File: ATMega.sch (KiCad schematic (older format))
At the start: 28 parts, among them J12 Conn_02x03_Odd_Even, SW1 SW_Push, U3 ATmega2560-16AU, Y1 16MHz

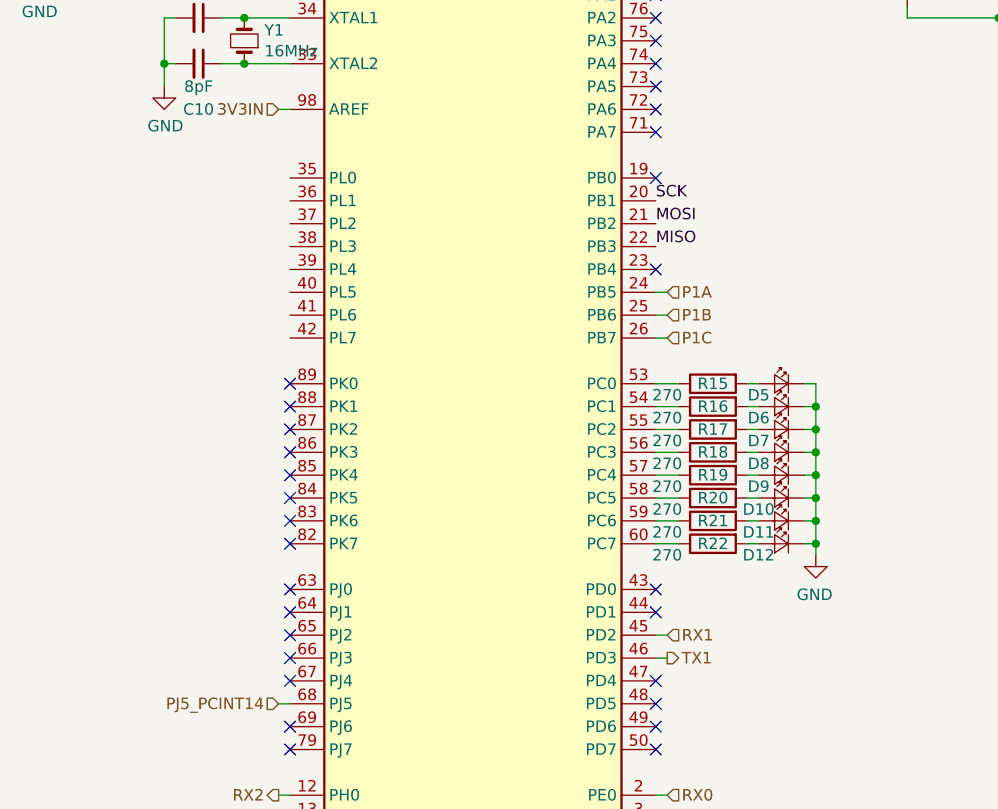
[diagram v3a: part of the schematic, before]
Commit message: LED, Mounting Holes
LEDs to register L
Mounting Holes
XT30
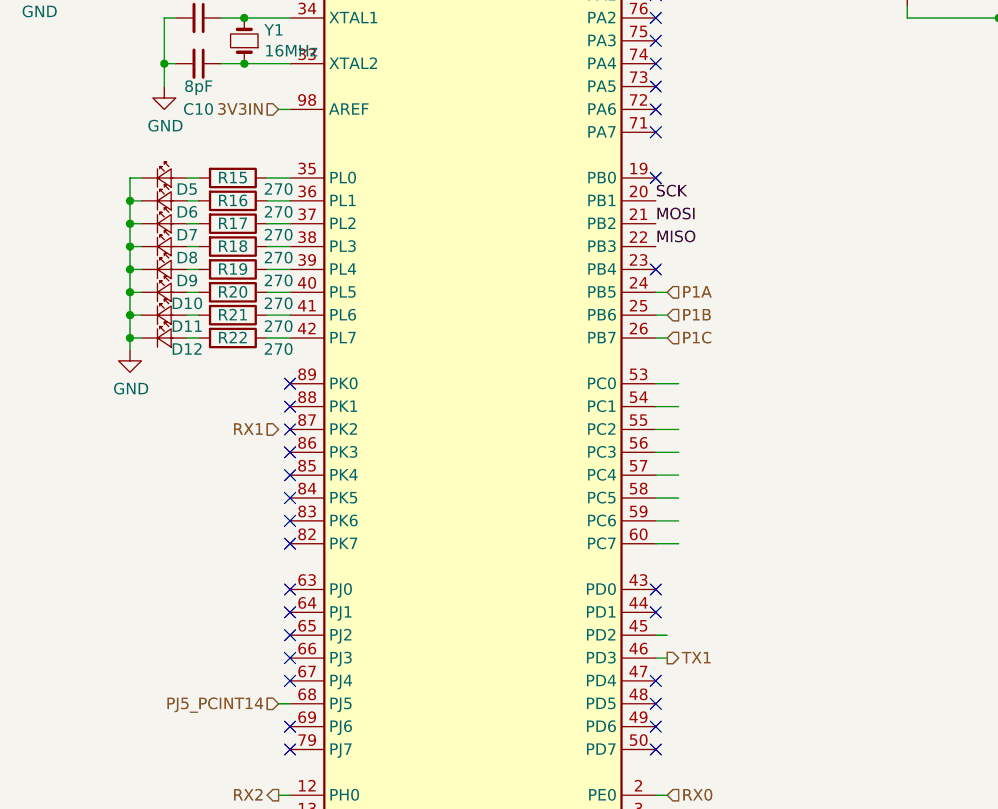
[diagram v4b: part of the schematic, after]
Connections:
- wire segments 95 -> 103
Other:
- moved on the sheet: D10, D11, D12, D5, D6, D7, D8, D9, R15, R16, R17, R18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

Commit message: layout
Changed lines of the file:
@@
 Wire Wire Line
 	4250 3550 4350 3550
-Text HLabel 2600 3350 0    50   Input ~ 0
+Text HLabel 4300 4250 2    50   Input ~ 0
 RX1
 Text HLabel 4300 4350 2    50   Output ~ 0

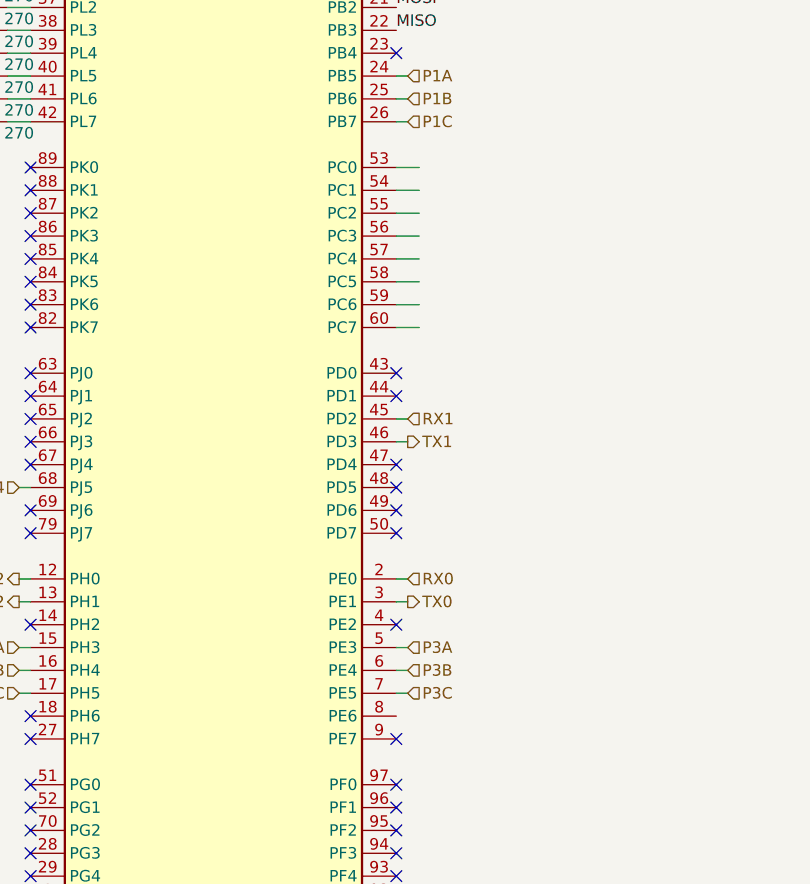
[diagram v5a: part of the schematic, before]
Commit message: added NCs to satisfy ERC
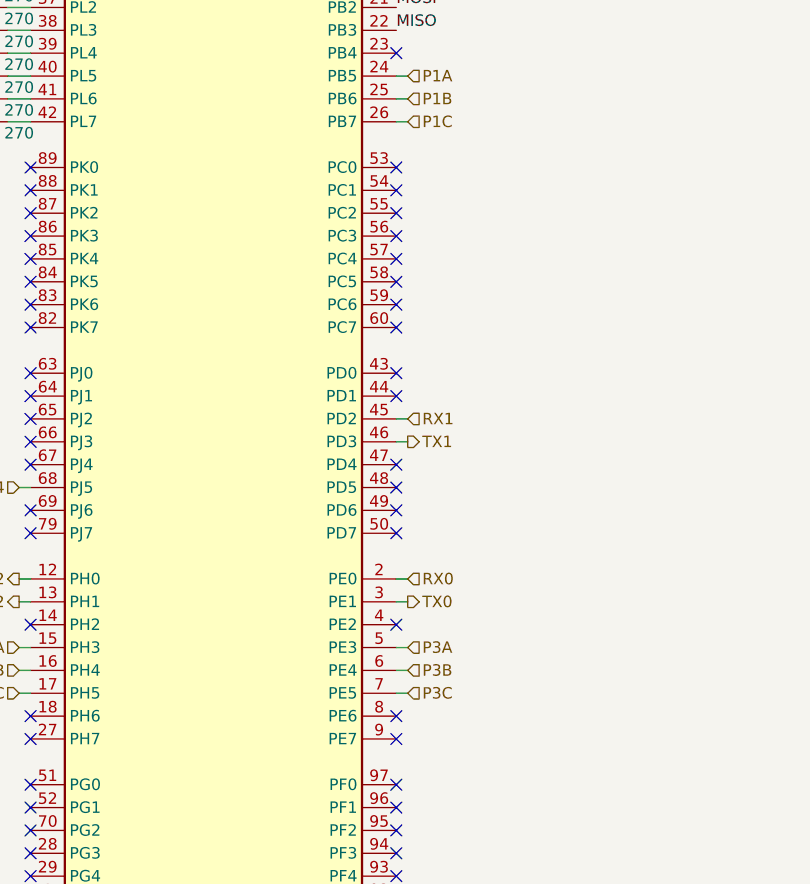
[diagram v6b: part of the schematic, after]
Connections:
- wire segments 103 -> 95
- no-connect marks 50 -> 59
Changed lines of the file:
@@
 	0    1    1    0
 $EndComp
-Wire Wire Line
-	4250 3150 4350 3150
-Wire Wire Line
-	4350 3250 4250 3250
-Wire Wire Line
-	4350 3350 4250 3350
-Wire Wire Line
-	4350 3450 4250 3450
 $Comp
 L Device:LED_Small D5
@@
 Wire Wire Line
 	1950 2950 1950 3000
-Wire Wire Line
-	4350 3850 4250 3850
-Wire Wire Line
-	4250 3750 4350 3750
-Wire Wire Line
-	4350 3650 4250 3650
-Wire Wire Line
-	4250 3550 4350 3550
 Text HLabel 4300 4250 2    50   Input ~ 0
 RX1
@@
 Wire Wire Line
 	2550 2950 2650 2950
+NoConn ~ 4250 3150
+NoConn ~ 4250 3250
+NoConn ~ 4250 3350
+NoConn ~ 4250 3450
+NoConn ~ 4250 3550
+NoConn ~ 4250 3650
+NoConn ~ 4250 3750
+NoConn ~ 4250 3850
+NoConn ~ 4250 5550
 $EndSCHEMATC

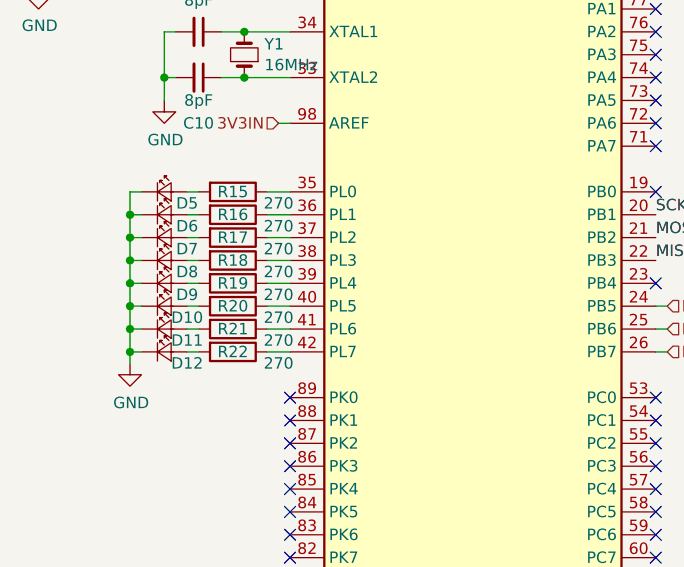
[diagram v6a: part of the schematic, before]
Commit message: fix LED resistor values
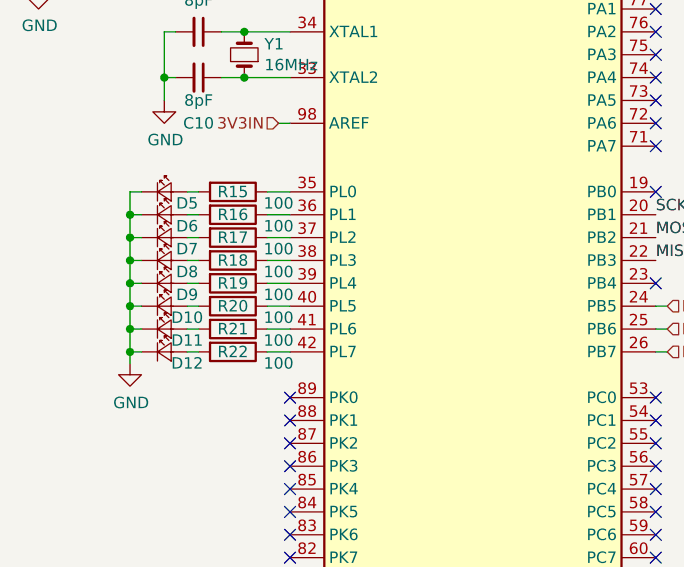
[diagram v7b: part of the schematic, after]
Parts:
- R15, R16, R17, R18, R19, R20, R21, R22: value 270 -> 100
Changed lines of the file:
@@
 P 2400 2350
 F 0 "R16" V 2400 2350 50  0000 C CNN
-F 1 "270" V 2450 2550 50  0000 C CNN
+F 1 "100" V 2450 2550 50  0000 C CNN
 F 2 "Resistor_SMD:R_0603_1608Metric" V 2330 2350 50  0001 C CNN
 F 3 "~" H 2400 2350 50  0001 C CNN
@@
 P 2400 2450
 F 0 "R17" V 2400 2450 50  0000 C CNN
-F 1 "270" V 2450 2650 50  0000 C CNN
+F 1 "100" V 2450 2650 50  0000 C CNN
 F 2 "Resistor_SMD:R_0603_1608Metric" V 2330 2450 50  0001 C CNN
 F 3 "~" H 2400 2450 50  0001 C CNN
@@
 P 2400 2550
 F 0 "R18" V 2400 2550 50  0000 C CNN
-F 1 "270" V 2450 2750 50  0000 C CNN
+F 1 "100" V 2450 2750 50  0000 C CNN
 F 2 "Resistor_SMD:R_0603_1608Metric" V 2330 2550 50  0001 C CNN
 F 3 "~" H 2400 2550 50  0001 C CNN
@@
 P 2400 2650
 F 0 "R19" V 2400 2650 50  0000 C CNN
-F 1 "270" V 2450 2850 50  0000 C CNN
+F 1 "100" V 2450 2850 50  0000 C CNN
 F 2 "Resistor_SMD:R_0603_1608Metric" V 2330 2650 50  0001 C CNN
 F 3 "~" H 2400 2650 50  0001 C CNN
@@
 P 2400 2750
 F 0 "R20" V 2400 2750 50  0000 C CNN
-F 1 "270" V 2450 2950 50  0000 C CNN
+F 1 "100" V 2450 2950 50  0000 C CNN
 F 2 "Resistor_SMD:R_0603_1608Metric" V 2330 2750 50  0001 C CNN
 F 3 "~" H 2400 2750 50  0001 C CNN
@@
 P 2400 2850
 F 0 "R21" V 2400 2850 50  0000 C CNN
-F 1 "270" V 2450 3050 50  0000 C CNN
+F 1 "100" V 2450 3050 50  0000 C CNN
 F 2 "Resistor_SMD:R_0603_1608Metric" V 2330 2850 50  0001 C CNN
 F 3 "~" H 2400 2850 50  0001 C CNN
@@
 P 2400 2950
 F 0 "R22" V 2400 2950 50  0000 C CNN
-F 1 "270" V 2450 3150 50  0000 C CNN
+F 1 "100" V 2450 3150 50  0000 C CNN
 F 2 "Resistor_SMD:R_0603_1608Metric" V 2330 2950 50  0001 C CNN
 F 3 "~" H 2400 2950 50  0001 C CNN
@@
 P 2400 2250
 F 0 "R15" V 2400 2250 50  0000 C CNN
-F 1 "270" V 2450 2450 50  0000 C CNN
+F 1 "100" V 2450 2450 50  0000 C CNN
 F 2 "Resistor_SMD:R_0603_1608Metric" V 2330 2250 50  0001 C CNN
 F 3 "~" H 2400 2250 50  0001 C CNN
